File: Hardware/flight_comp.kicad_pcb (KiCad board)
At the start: 4 copper layers, 86.7 x 48.2 mm, 127 parts, among them IC1 BMP388, IC4 TPS259531DSGR, J1 Conn_Coaxial, J10 CAMERA_CONN_01, J11 CAMERA_CONN_02, J12 Conn_Coaxial, J13 CAMERA_CONN_03, J2 TC2030, J3 XT30, J4 USB_C_Receptacle_USB2.0_16P, J5 Conn_01x02, J6 Conn_01x02, J7 SERVO_CONN_01, J8 SERVO_CONN_02, J9 SERVO_CONN_02, Q2 DMP3013SFV, Q3 CSD17577Q3A, Q4 CSD17577Q3A, Q5 PMBT2222A, SW1 NRST, SW2 BOOT0, SW3 EG2219, U1 STM32F405RGTx, U10 LTC4412, U11 UCC27517A, U12 UCC27517A, U13 LSM6DSO, U2 MAX-M10S, U3 74LVC1GU04, U4 W25Q32JVSS, U5 24LC64, U6 MP2331, U7 AMS1117-5.0, U8 USBLC6-2SC6, Y1 8mHz, Y2 32.768 kHz

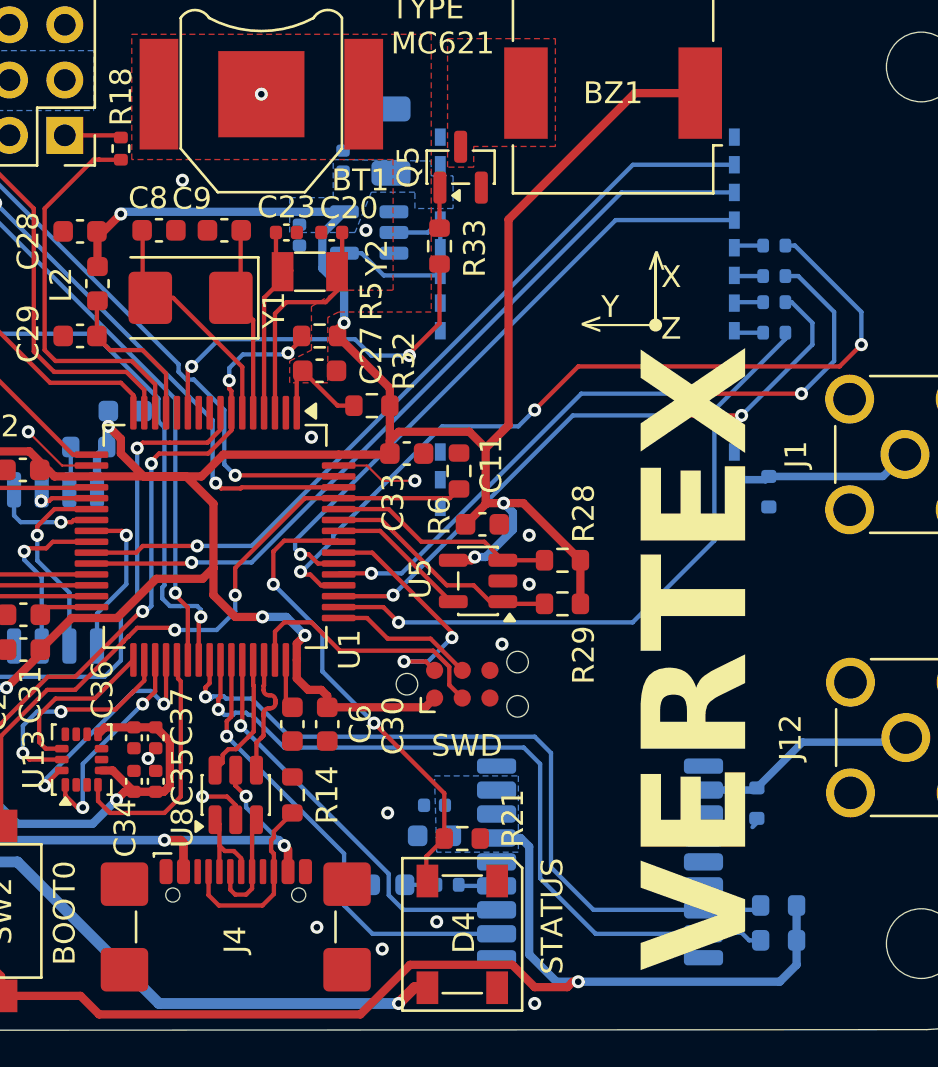
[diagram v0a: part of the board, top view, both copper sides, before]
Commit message: GPS antenna connections, pps is connected to the mcu, pps diode replaced
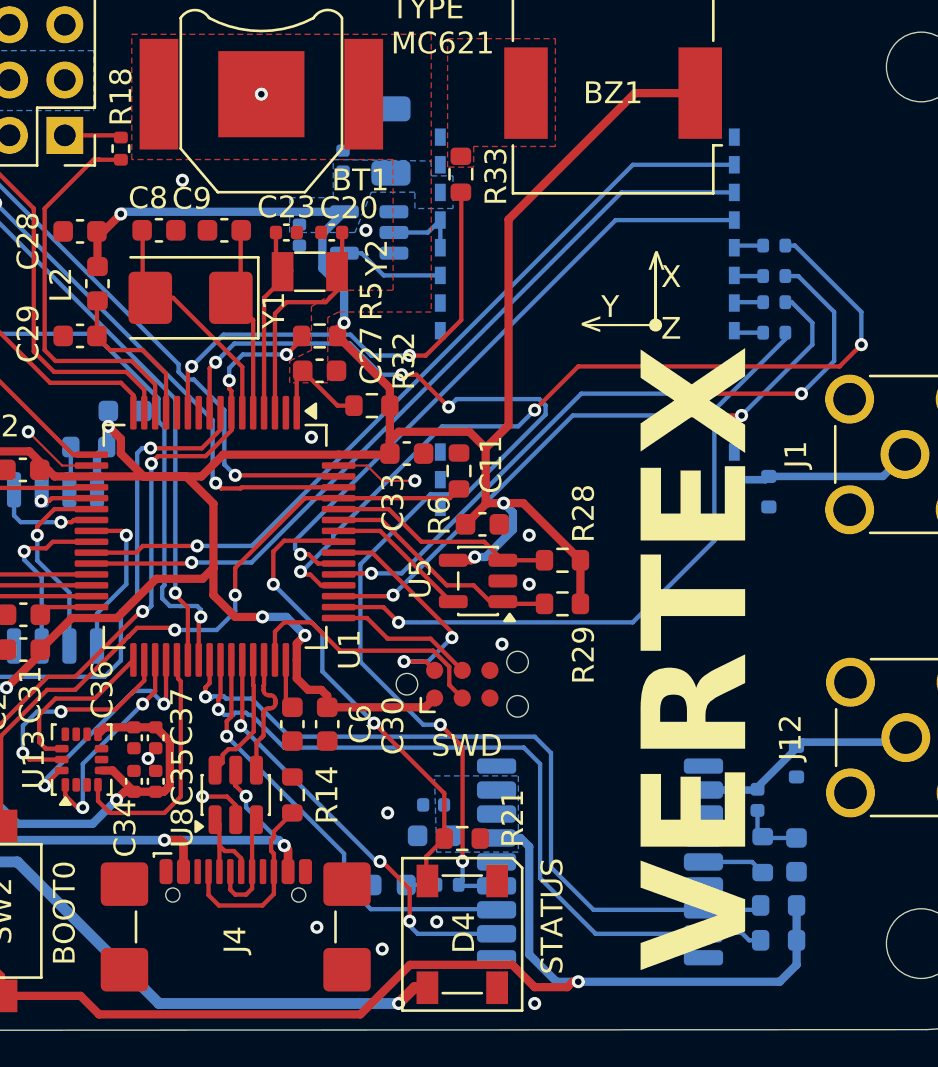
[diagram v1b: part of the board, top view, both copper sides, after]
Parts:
- removed Q5: PMBT2222A, Package_TO_SOT_SMD:SOT-23
- removed TX4: XL-1608UBC-04, LED_SMD:LED_0603_1608Metric
- added C38: 10nF, Capacitor_SMD:C_0603_1608Metric, B.Cu at (151.2, 121.8)
- added D7: LED, LED_SMD:LED_0603_1608Metric, B.Cu at (132.5, 123.2)
- added FB1: LQG15HS27NH02D, Inductor_SMD:L_0402_1005Metric, B.Cu at (149.4, 119.2)
- added R35: 10, Resistor_SMD:R_0603_1608Metric, B.Cu at (149.7, 121.8)
- moved R33 3.44 mm to (135.8, 90.5)
- moved D5 2.63 mm to (151.2, 117.5)
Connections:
- R33 pad 2: Net-(Q5-B) -> Net-(BZ1--)
- R48 pad 2: Net-(U2-TIMEPULSE) -> PPS
- U1 pad 9: unconnected-(U1-PC1-Pad9) -> PPS
- U2 pad 14: unconnected-(U2-VCC_RF-Pad14) -> Net-(U2-VCC_RF)
- U2 pad 15: GND -> unconnected-(U2-VIO_SEL-Pad15)
- U2 pad 2: GPS_TX -> GPS_RX
- U2 pad 3: GPS_RX -> GPS_TX
- U2 pad 4: Net-(U2-TIMEPULSE) -> PPS
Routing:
- net PPS: track 0.00 -> 50.2 mm, vias 0 -> 5
- net BUZZ: track 17.8 -> 22.1 mm
- net Net-(U2-VCC_RF): track 0.00 -> 2.92 mm
- net Net-(C38-Pad1): track 0.00 -> 2.88 mm
- net Net-(Q5-B): track 1.87 -> 0.00 mm
- net Net-(U2-TIMEPULSE): track 1.84 -> 0.00 mm
- net GPS_TX: track 21.1 -> 20.1 mm
- net GPS_RX: track 18.9 -> 19.8 mm, vias 1 -> 3
